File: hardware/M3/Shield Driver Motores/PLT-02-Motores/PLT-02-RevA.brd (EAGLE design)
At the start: 68.6 x 53.6 mm, 17 parts

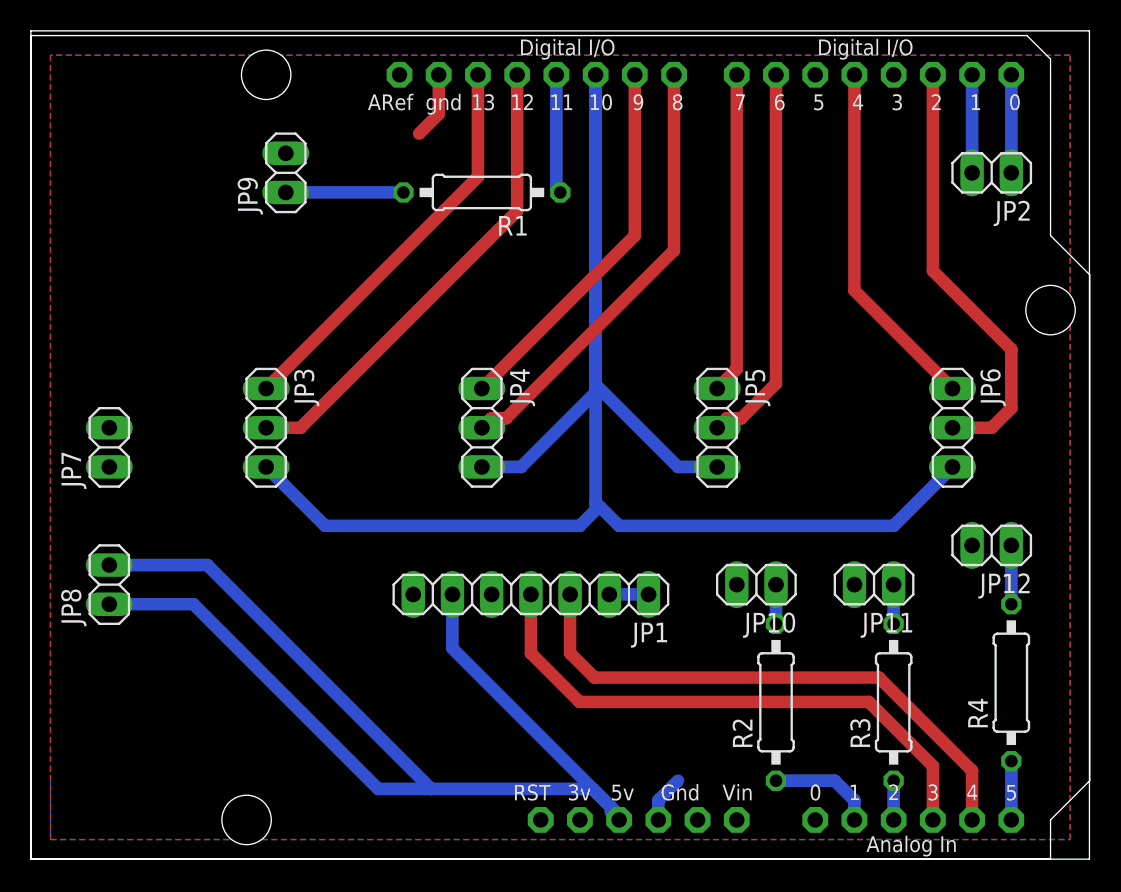
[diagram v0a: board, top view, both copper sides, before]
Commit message: Se hacen algunas correcciones en placa subida por LL
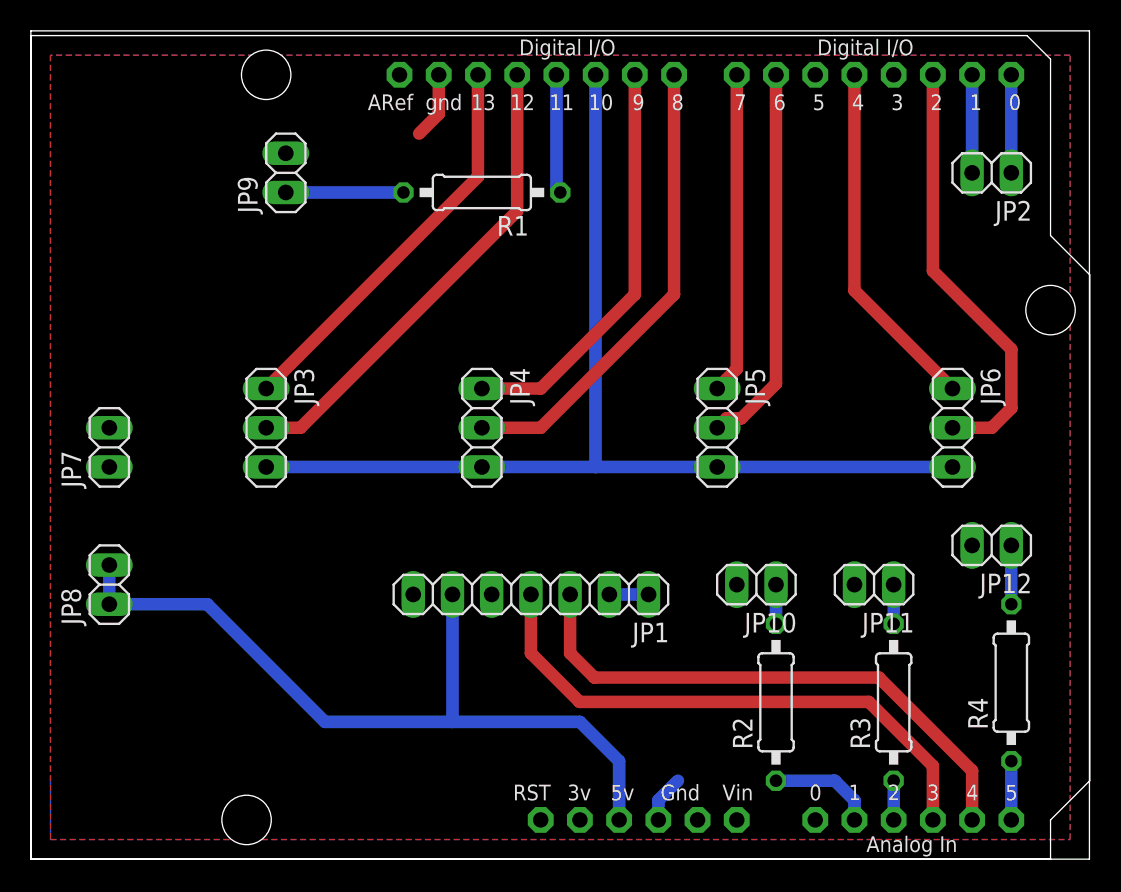
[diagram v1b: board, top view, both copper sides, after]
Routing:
- net D10: track 136.9 -> 69.8 mm
- net 5V: track 84.9 -> 51.8 mm
- net D9: track 24.4 -> 26.7 mm
- net D8: track 28.6 -> 30.2 mm
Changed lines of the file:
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@@
 <contactref element="JP8" pad="1"/>
 <contactref element="JP8" pad="2"/>
-<wire x1="46.99" y1="6.35" x2="46.99" y2="6.668" width="0.8128" layer="16"/>
-<wire x1="46.99" y1="6.668" x2="36.195" y2="17.463" width="0.8128" layer="16"/>
-<wire x1="36.195" y1="20.955" x2="36.195" y2="17.463" width="0.8128" layer="16"/>
-<wire x1="13.97" y1="22.86" x2="20.32" y2="22.86" width="0.8128" layer="16"/>
-<wire x1="13.97" y1="20.32" x2="19.4183" y2="20.32" width="0.8128" layer="16"/>
-<wire x1="19.4183" y1="20.32" x2="31.3817" y2="8.3566" width="0.8128" layer="16"/>
-<wire x1="31.3817" y1="8.3566" x2="34.8234" y2="8.3566" width="0.8128" layer="16"/>
-<wire x1="45.2811625" y1="8.3566" x2="46.4566" y2="7.1811625" width="0.8128" layer="16"/>
-<wire x1="46.4566" y1="7.1811625" x2="46.4566" y2="6.8834" width="0.8128" layer="16"/>
-<wire x1="46.4566" y1="6.8834" x2="46.99" y2="6.35" width="0.8128" layer="16"/>
-<wire x1="20.32" y1="22.86" x2="34.8234" y2="8.3566" width="0.8128" layer="16"/>
-<wire x1="34.8234" y1="8.3566" x2="45.2811625" y2="8.3566" width="0.8128" layer="16"/>
+<wire x1="46.99" y1="6.35" x2="46.99" y2="10.16" width="0.8128" layer="16"/>
+<wire x1="46.99" y1="10.16" x2="44.45" y2="12.7" width="0.8128" layer="16"/>
+<wire x1="27.94" y1="12.7" x2="20.32" y2="20.32" width="0.8128" layer="16"/>
+<wire x1="44.45" y1="12.7" x2="36.195" y2="12.7" width="0.8128" layer="16"/>
+<wire x1="36.195" y1="12.7" x2="27.94" y2="12.7" width="0.8128" layer="16"/>
+<wire x1="20.32" y1="20.32" x2="13.97" y2="20.32" width="0.8128" layer="16"/>
+<wire x1="36.195" y1="20.955" x2="36.195" y2="12.7" width="0.8128" layer="16"/>
+<wire x1="13.97" y1="22.86" x2="13.97" y2="20.32" width="0.8128" layer="16"/>
 </signal>
 <signal name="D2">
@@
 <contactref element="U$1" pad="D8"/>
 <contactref element="JP4" pad="2"/>
-<wire x1="38.1" y1="31.75" x2="38.7096" y2="32.3596" width="0.8128" layer="1"/>
-<wire x1="38.7096" y1="32.3596" x2="39.6616" y2="32.3596" width="0.8128" layer="1"/>
-<wire x1="39.6616" y1="32.3596" x2="50.546" y2="43.244" width="0.8128" layer="1"/>
-<wire x1="50.546" y1="43.244" x2="50.546" y2="54.61" width="0.8128" layer="1"/>
+<wire x1="38.1" y1="31.75" x2="41.91" y2="31.75" width="0.8128" layer="1"/>
+<wire x1="41.91" y1="31.75" x2="50.546" y2="40.386" width="0.8128" layer="1"/>
+<wire x1="50.546" y1="40.386" x2="50.546" y2="54.61" width="0.8128" layer="1"/>
 </signal>
 <signal name="D9">
 <contactref element="U$1" pad="D9"/>
 <contactref element="JP4" pad="1"/>
-<wire x1="38.1" y1="34.29" x2="48.006" y2="44.196" width="0.8128" layer="1"/>
-<wire x1="48.006" y1="44.196" x2="48.006" y2="54.61" width="0.8128" layer="1"/>
+<wire x1="48.006" y1="40.386" x2="41.91" y2="34.29" width="0.8128" layer="1"/>
+<wire x1="41.91" y1="34.29" x2="38.1" y2="34.29" width="0.8128" layer="1"/>
+<wire x1="48.006" y1="54.61" x2="48.006" y2="40.386" width="0.8128" layer="1"/>
 </signal>
 <signal name="D10">
@@
 <contactref element="JP5" pad="3"/>
 <contactref element="JP6" pad="3"/>
-<wire x1="68.58" y1="29.21" x2="64.77" y2="25.4" width="0.8128" layer="16"/>
-<wire x1="64.77" y1="25.4" x2="46.99" y2="25.4" width="0.8128" layer="16"/>
-<wire x1="46.99" y1="25.4" x2="45.466" y2="26.924" width="0.8128" layer="16"/>
-<wire x1="45.466" y1="26.924" x2="45.466" y2="54.61" width="0.8128" layer="16"/>
-<wire x1="45.466" y1="34.036" x2="40.64" y2="29.21" width="0.8128" layer="16"/>
-<wire x1="38.1" y1="29.21" x2="40.64" y2="29.21" width="0.8128" layer="16"/>
-<wire x1="45.466" y1="54.61" x2="45.466" y2="34.036" width="0.8128" layer="16"/>
-<wire x1="53.34" y1="29.21" x2="50.8000125" y2="29.21" width="0.8128" layer="16"/>
-<wire x1="50.8000125" y1="29.21" x2="45.466" y2="34.54406875" width="0.8128" layer="16"/>
-<wire x1="45.466" y1="34.54406875" x2="45.466" y2="54.61" width="0.8128" layer="16"/>
-<wire x1="24.13" y1="29.21" x2="27.94" y2="25.4" width="0.8128" layer="16"/>
-<wire x1="27.94" y1="25.4" x2="44.45" y2="25.4" width="0.8128" layer="16"/>
-<wire x1="44.45" y1="25.4" x2="45.466" y2="26.416" width="0.8128" layer="16"/>
-<wire x1="45.466" y1="26.416" x2="45.466" y2="26.924" width="0.8128" layer="16"/>
+<wire x1="38.1" y1="29.21" x2="45.466" y2="29.21" width="0.8128" layer="16"/>
+<wire x1="53.34" y1="29.21" x2="45.466" y2="29.21" width="0.8128" layer="16"/>
+<wire x1="45.466" y1="54.61" x2="45.466" y2="29.21" width="0.8128" layer="16"/>
+<wire x1="24.13" y1="29.21" x2="38.1" y2="29.21" width="0.8128" layer="16"/>
+<wire x1="53.34" y1="29.21" x2="68.58" y2="29.21" width="0.8128" layer="16"/>
 </signal>
 <signal name="D7">
